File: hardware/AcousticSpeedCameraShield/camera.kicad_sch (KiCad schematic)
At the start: 8 parts

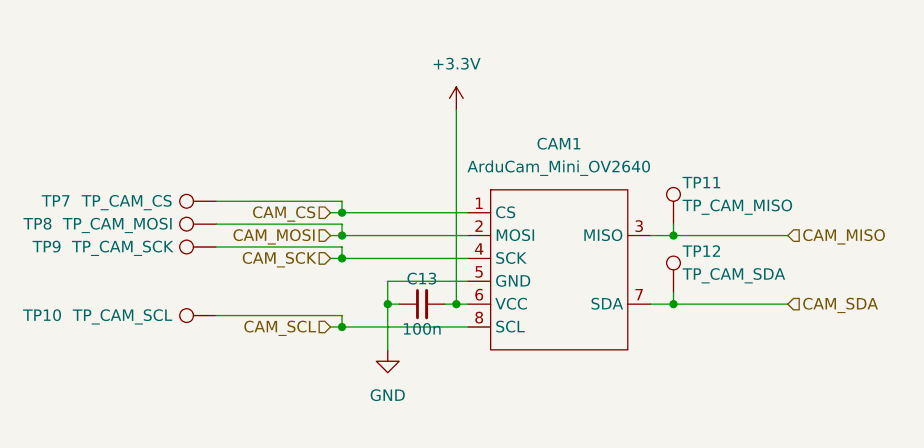
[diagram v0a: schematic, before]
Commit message: update MCU pin assignments
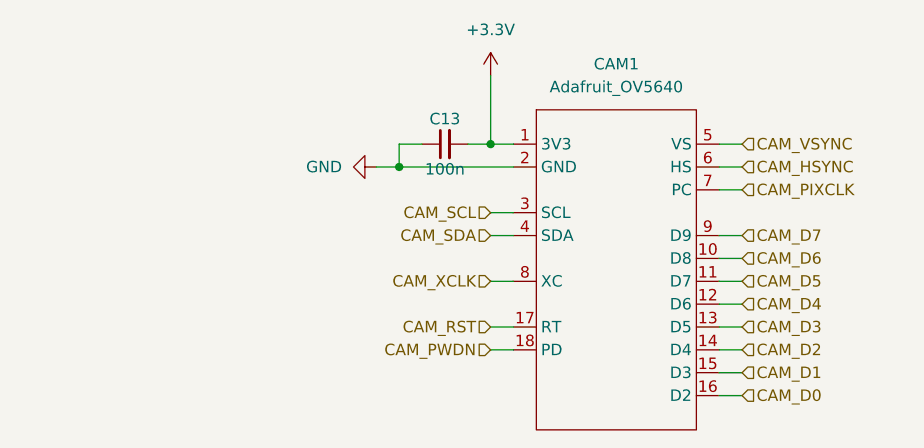
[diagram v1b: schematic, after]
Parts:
- removed CAM1: ArduCam_Mini_OV2640, Connector_PinSocket_2.54mm:PinSocket_1x08_P2.54mm_Vertical, symbol AcousticSpeedCamera:ArduCam_Mini_OV2640
- removed TP10: TP_CAM_SCL, symbol Connector:TestPoint
- removed TP11: TP_CAM_MISO, symbol Connector:TestPoint
- removed TP12: TP_CAM_SDA, symbol Connector:TestPoint
- removed TP7: TP_CAM_CS, symbol Connector:TestPoint
- removed TP8: TP_CAM_MOSI, symbol Connector:TestPoint
- removed TP9: TP_CAM_SCK, symbol Connector:TestPoint
- added CAM1: Adafruit_OV5640, Connector_PinSocket_2.54mm:PinSocket_2x09_P2.54mm_Vertical, symbol AcousticSpeedCamera:Adafruit_OV5640
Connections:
- net +3.3V: now also CAM1.1 (3V3)
- net CAM_SCL: now also CAM1.3 (SCL)
- net CAM_SDA: now also CAM1.4 (SDA)
- net GND: now also CAM1.2 (GND)
- new net CAM_D0: CAM1.16 (D2)
- new net CAM_D1: CAM1.15 (D3)
- new net CAM_D2: CAM1.14 (D4)
- new net CAM_D3: CAM1.13 (D5)
- new net CAM_D4: CAM1.12 (D6)
- new net CAM_D5: CAM1.11 (D7)
- new net CAM_D6: CAM1.10 (D8)
- new net CAM_D7: CAM1.9 (D9)
- new net CAM_HSYNC: CAM1.6 (HS)
- new net CAM_PIXCLK: CAM1.7 (PC)
- new net CAM_PWDN: CAM1.18 (PD)
- new net CAM_RST: CAM1.17 (RT)
- new net CAM_VSYNC: CAM1.5 (VS)
- new net CAM_XCLK: CAM1.8 (XC)
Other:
- title: (none) -> Interfejs Kamery
- moved on the sheet: C13
